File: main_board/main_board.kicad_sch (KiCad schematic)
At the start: 96 parts, among them J1 3.5mm Jack, J18 Conn_01x15_Female, J19 Conn_01x15_Female, J2 3.5mm Jack, J20 Conn_01x02_Male, J21 OLED Pins, J3 3.5mm Jack, J4 3.5mm Jack, J5 Display Header, J6 EU Power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

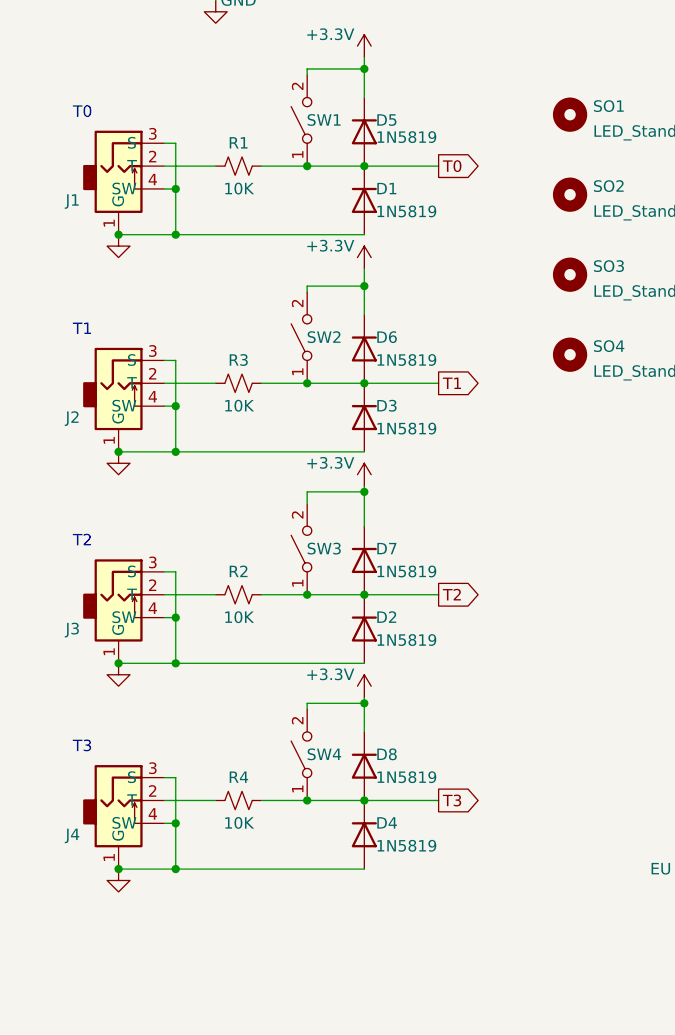
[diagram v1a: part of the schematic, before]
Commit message: Adds debounce caps to trigger inputs
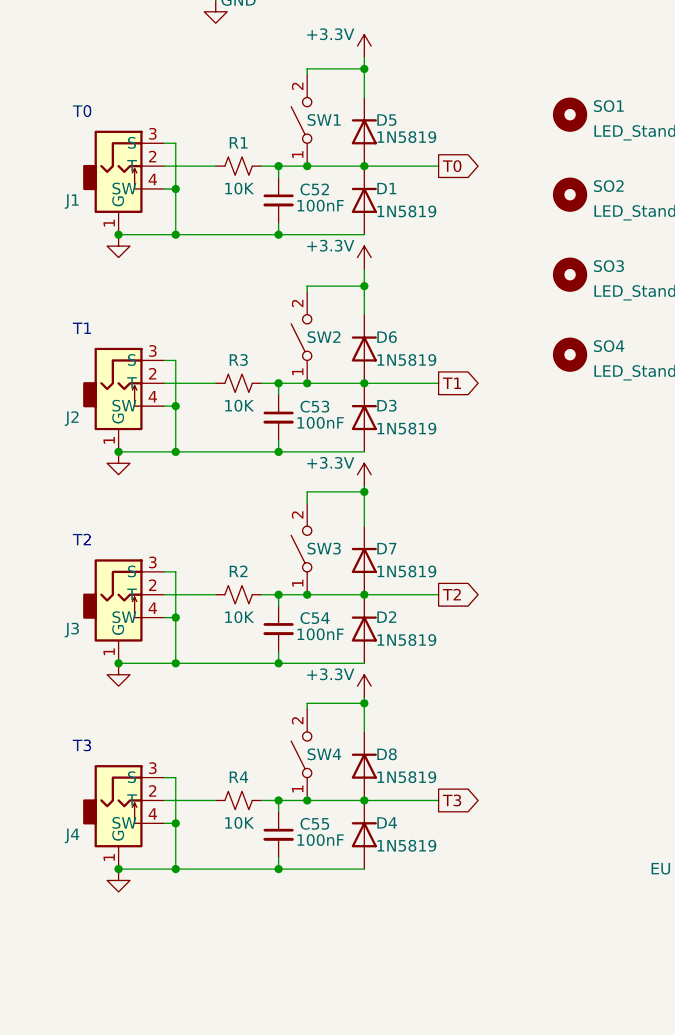
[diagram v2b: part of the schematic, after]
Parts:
- added C52, C53, C54, C55: 100nF, Capacitor_SMD:C_0805_2012Metric_Pad1.18x1.45mm_HandSolder, symbol Device:C_Small
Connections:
- net GND: now also C52.2, C53.2, C54.2, C55.2
- net T0: now also C52.1
- net T1: now also C53.1
- net T2: now also C54.1
- net T3: now also C55.1

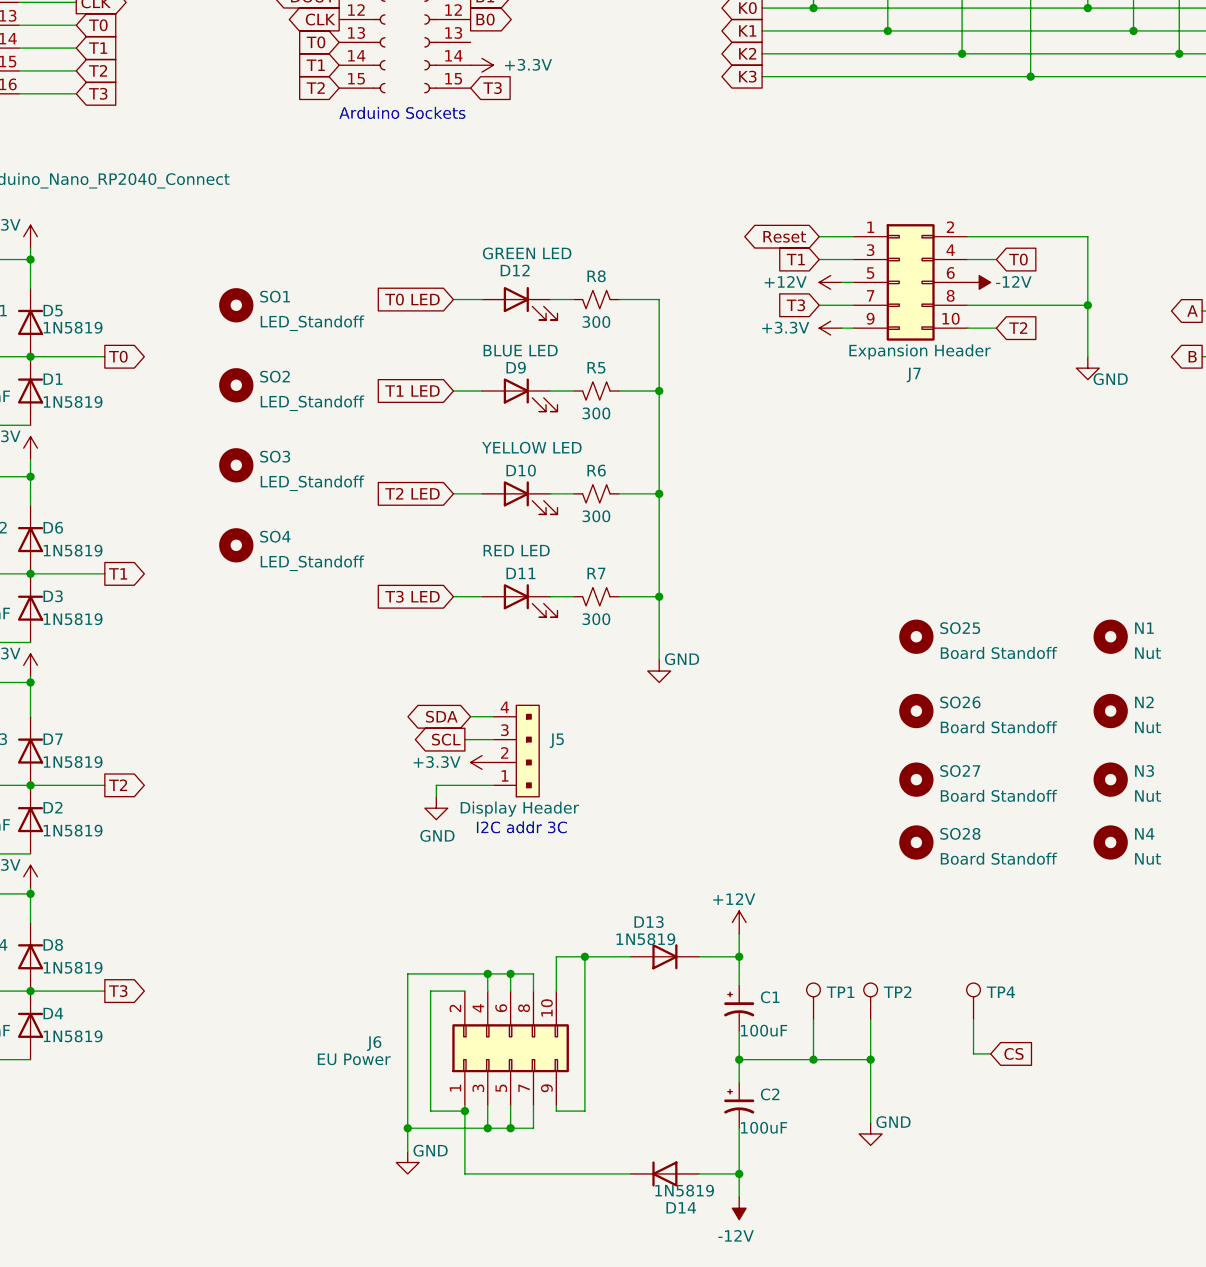
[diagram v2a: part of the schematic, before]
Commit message: Updates main_board, uses generate_boms.bat
Updates reverse protection circuitry on main board.
Updates 3.3V reference circuitry.
Uses generate_boms and retires .xlsx BOM files.
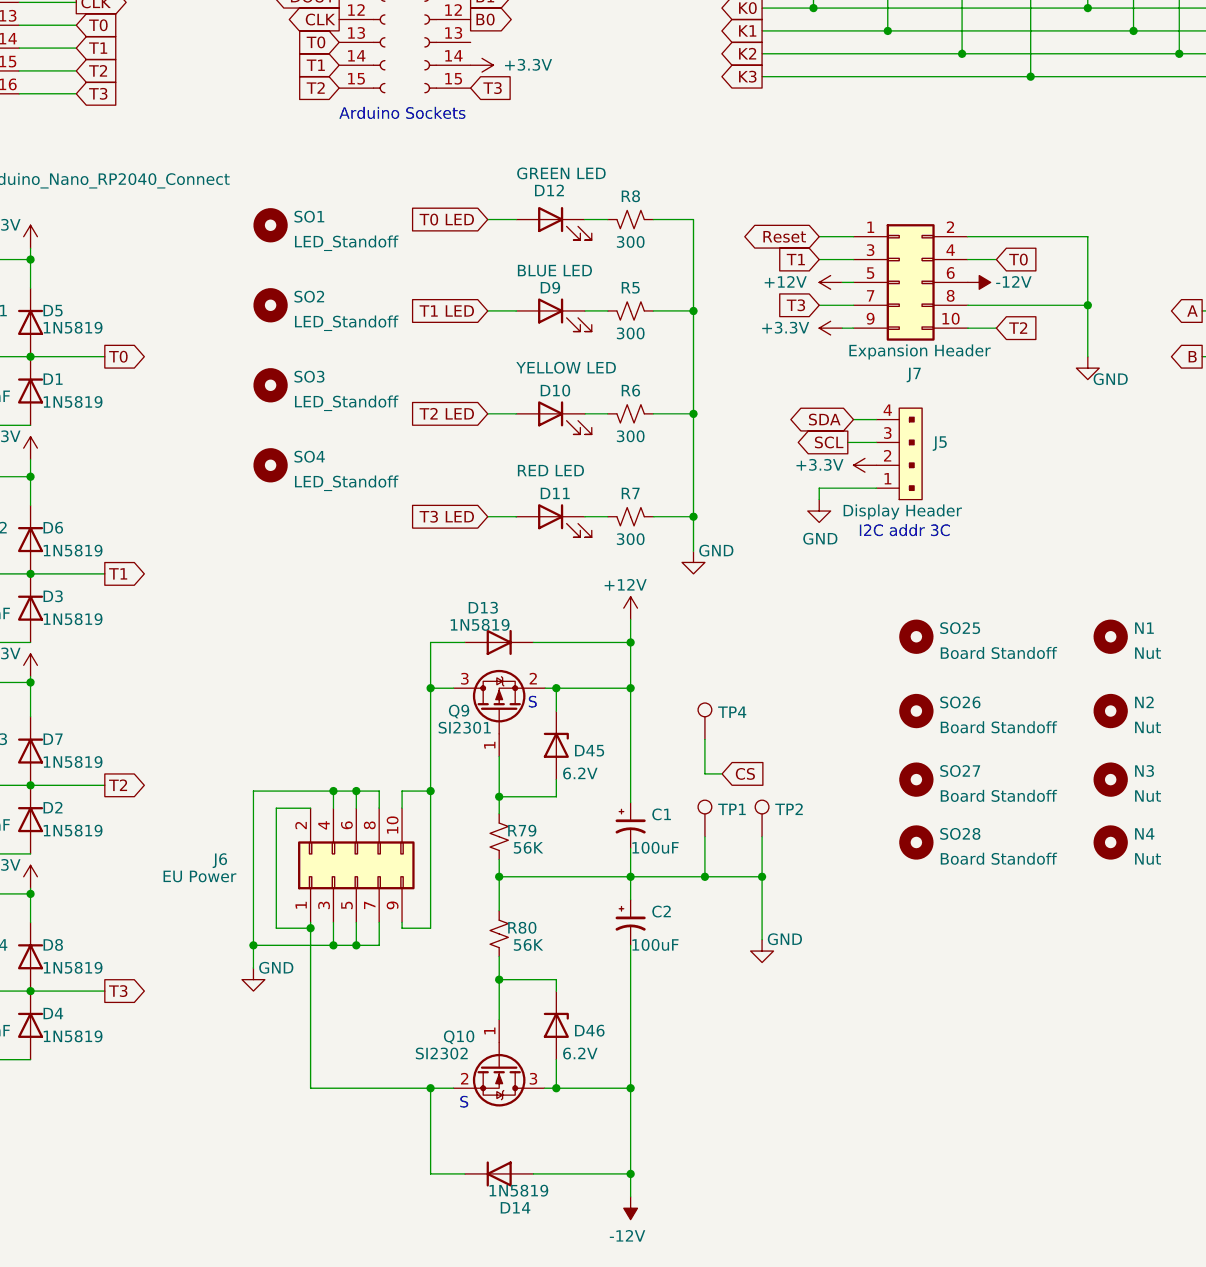
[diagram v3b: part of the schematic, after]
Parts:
- added D45, D46: 6.2V, Diode_SMD:D_SOD-323, symbol Diode:BZX384-xxx
- added Q10: SI2302, Package_TO_SOT_SMD:SOT-23, symbol Transistor_FET:2N7002
- added Q9: SI2301, Package_TO_SOT_SMD:SOT-23, symbol Transistor_FET:Si2371EDS
- added R79, R80: 56K, Resistor_SMD:R_0603_1608Metric, symbol Device:R_Small_US
- C1, C2:  LCSC Part # C2887272 -> (none); LCSC Part # (none) -> C2887272
- C11, C12:  LCSC Part # C1710 -> (none); LCSC Part # (none) -> C1710
- C30, C34, C52, C53, C54, C55:  LCSC Part # C49678 -> (none); LCSC Part # (none) -> C49678
- C7:  LCSC Part # C28323 -> (none); LCSC Part # (none) -> C28323
- D1, D13, D14, D2, D3, D4, D5, D6, D7, D8:  LCSC Part # C191023 -> (none); LCSC Part # (none) -> C191023
- J18, J19:  LCSC Part # C2932676 -> (none); LCSC Part # (none) -> C2932676
- J20:  LCSC Part # C492401 -> (none); LCSC Part # (none) -> C492401
- J6, J7:  LCSC Part # C115170 -> (none); LCSC Part # (none) -> C115170
- R1, R125, R126, R127, R128, R2, R3, R4, R66, R67, R68:  LCSC Part # C17414 -> (none); LCSC Part # (none) -> C17414
- R5, R6, R7, R8:  LCSC Part # C17617 -> (none); LCSC Part # (none) -> C17617
- TP1, TP2:  LCSC Part # C2906764 -> (none); LCSC Part # (none) -> C2906764
- TP4:  LCSC Part # C238123 -> (none); LCSC Part # (none) -> C238123
- U16:  LCSC Part # C47538 -> (none); LCSC Part # (none) -> C47538
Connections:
- net +12V: now also D45.1 (K), Q9.2 (S)
- net -12V: now also D46.2 (A), Q10.3 (D)
- net GND: now also R79.2, R80.1
- net at D13.2 (A), J6.10 (Pin_10), J6.9 (Pin_9): now also Q9.3 (D)
- net at D14.1 (K), J6.1 (Pin_1), J6.2 (Pin_2): now also Q10.2 (S)
- new net: D46.1 (K), Q10.1 (G), R80.2
- new net: D45.2 (A), Q9.1 (G), R79.1
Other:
- note added: "S"
- moved on the sheet: C1, C2, D10, D11, D12, D13, D14, D9, J5, J6, R5, R6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

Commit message: Rev 4.2 of board
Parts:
- J6, J7: LCSC Part # C115170 -> C492422
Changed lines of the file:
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@@
       (effects (font (size 1.27 1.27)) hide)
     )
-    (property "LCSC Part #" "C115170" (id 5) (at 152.4 87.63 0)
+    (property "LCSC Part #" "C492422" (id 5) (at 152.4 87.63 0)
       (effects (font (size 1.27 1.27)) hide)
     )
@@
       (effects (font (size 1.27 1.27)) hide)
     )
-    (property "LCSC Part #" "C115170" (id 5) (at 92.075 153.67 0)
+    (property "LCSC Part #" "C492422" (id 5) (at 92.075 153.67 0)
       (effects (font (size 1.27 1.27)) hide)
     )
@@
     )
     (path "/b200c1d4-b772-4a0d-a7bc-c10bcb241496/da91d24c-235c-487e-8a89-c861581e141b"
-      (reference "U13") (unit 1) (value "DG412xY") (footprint "Package_SO:SOIC-16_3.9x9.9mm_P1.27mm")
+      (reference "U13") (unit 1) (value "DG412DY-E3") (footprint "Package_SO:SOIC-16_3.9x9.9mm_P1.27mm")
     )
     (path "/b200c1d4-b772-4a0d-a7bc-c10bcb241496/4d86a335-e2f3-43e1-bfbb-9bbbf85afd83"
-      (reference "U13") (unit 2) (value "DG412xY") (footprint "Package_SO:SOIC-16_3.9x9.9mm_P1.27mm")
+      (reference "U13") (unit 2) (value "DG412DY-E3") (footprint "Package_SO:SOIC-16_3.9x9.9mm_P1.27mm")
     )
     (path "/b200c1d4-b772-4a0d-a7bc-c10bcb241496/4c813f4a-7d60-4bf9-a697-cffeff5134b5"
-      (reference "U13") (unit 3) (value "DG412xY") (footprint "Package_SO:SOIC-16_3.9x9.9mm_P1.27mm")
+      (reference "U13") (unit 3) (value "DG412DY-E3") (footprint "Package_SO:SOIC-16_3.9x9.9mm_P1.27mm")
     )
     (path "/b200c1d4-b772-4a0d-a7bc-c10bcb241496/87c697e6-3b77-4484-9517-8dc7c9b0f1d4"
-      (reference "U13") (unit 4) (value "DG412xY") (footprint "Package_SO:SOIC-16_3.9x9.9mm_P1.27mm")
+      (reference "U13") (unit 4) (value "DG412DY-E3") (footprint "Package_SO:SOIC-16_3.9x9.9mm_P1.27mm")
     )
     (path "/b200c1d4-b772-4a0d-a7bc-c10bcb241496/2c3bee7b-576b-4f00-aba9-231f47c1ce9c"
-      (reference "U13") (unit 5) (value "DG412xY") (footprint "Package_SO:SOIC-16_3.9x9.9mm_P1.27mm")
+      (reference "U13") (unit 5) (value "DG412DY-E3") (footprint "Package_SO:SOIC-16_3.9x9.9mm_P1.27mm")
     )
     (path "/eae55a42-d110-46e1-b06f-560b3d6a7f91/a5b41785-6602-47dd-88c9-fe5b8067460e"
@@
     )
     (path "/b200c1d4-b772-4a0d-a7bc-c10bcb241496/014b02a6-58b3-4f97-b161-484c3f4529db"
-      (reference "U24") (unit 1) (value "DG412xY") (footprint "Package_SO:SOIC-16_3.9x9.9mm_P1.27mm")
+      (reference "U24") (unit 1) (value "DG412DY-E3") (footprint "Package_SO:SOIC-16_3.9x9.9mm_P1.27mm")
     )
     (path "/b200c1d4-b772-4a0d-a7bc-c10bcb241496/9f9d1f6f-7507-4bd1-b7c3-1eb7cae036e5"
-      (reference "U24") (unit 2) (value "DG412xY") (footprint "Package_SO:SOIC-16_3.9x9.9mm_P1.27mm")
+      (reference "U24") (unit 2) (value "DG412DY-E3") (footprint "Package_SO:SOIC-16_3.9x9.9mm_P1.27mm")
     )
     (path "/b200c1d4-b772-4a0d-a7bc-c10bcb241496/0ef053cc-6cbc-480a-97da-ffd86eed29bd"
-      (reference "U24") (unit 3) (value "DG412xY") (footprint "Package_SO:SOIC-16_3.9x9.9mm_P1.27mm")
+      (reference "U24") (unit 3) (value "DG412DY-E3") (footprint "Package_SO:SOIC-16_3.9x9.9mm_P1.27mm")
     )
     (path "/b200c1d4-b772-4a0d-a7bc-c10bcb241496/f9466c72-e334-45f8-ab36-33d7247619a7"
-      (reference "U24") (unit 4) (value "DG412xY") (footprint "Package_SO:SOIC-16_3.9x9.9mm_P1.27mm")
+      (reference "U24") (unit 4) (value "DG412DY-E3") (footprint "Package_SO:SOIC-16_3.9x9.9mm_P1.27mm")
     )
     (path "/b200c1d4-b772-4a0d-a7bc-c10bcb241496/56818c14-9875-4852-83e7-b24bf77170c1"
-      (reference "U24") (unit 5) (value "DG412xY") (footprint "Package_SO:SOIC-16_3.9x9.9mm_P1.27mm")
-    )
-  )
+      (reference "U24") (unit 5) (value "DG412DY-E3") (footprint "Package_SO:SOIC-16_3.9x9.9mm_P1.27mm")
+    )
+  )

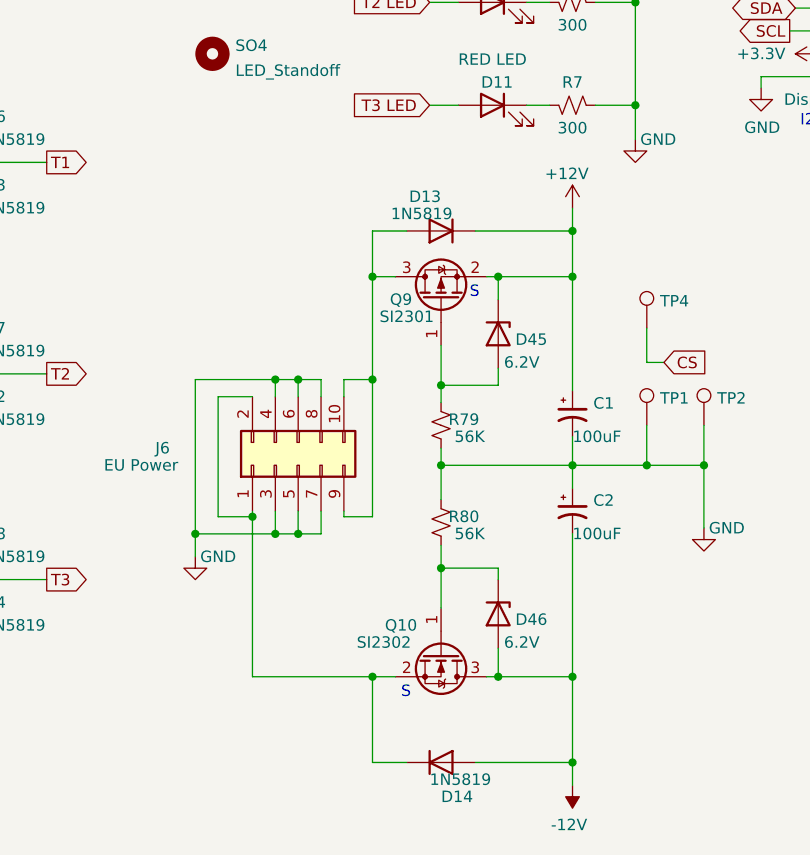
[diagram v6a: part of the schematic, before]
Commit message: Goes to diodes for reverse power protection
Re-layout for better noise performance.
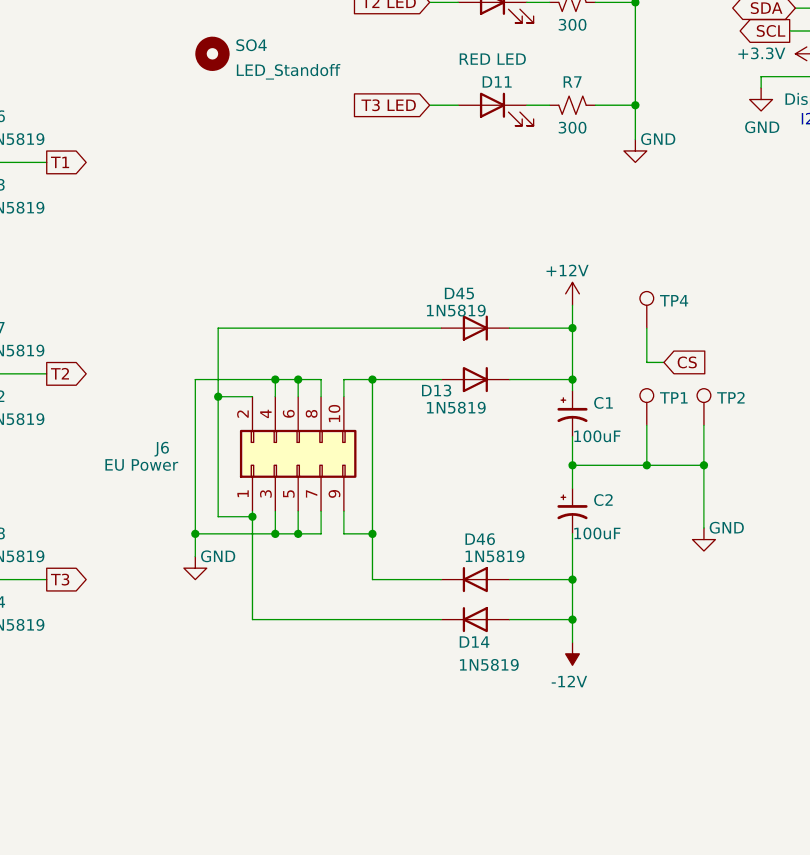
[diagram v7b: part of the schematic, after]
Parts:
- removed D45, D46: 6.2V, Diode_SMD:D_SOD-323, symbol Diode:BZX384-xxx
- removed Q10: SI2302, Package_TO_SOT_SMD:SOT-23, symbol Transistor_FET:2N7002
- removed Q9: SI2301, Package_TO_SOT_SMD:SOT-23, symbol Transistor_FET:Si2371EDS
- removed R79, R80: 56K, Resistor_SMD:R_0603_1608Metric, symbol Device:R_Small_US
- added D45, D46: 1N5819, Diode_SMD:D_0805_2012Metric_Pad1.15x1.40mm_HandSolder, symbol Diode:1N4148
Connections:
- net +12V: now also D45.1 (K)
- net -12V: now also D46.2 (A)
- net at D13.2 (A), J6.10 (Pin_10), J6.9 (Pin_9): now also D46.1 (K)
- net at D14.1 (K), J6.1 (Pin_1), J6.2 (Pin_2): now also D45.2 (A)
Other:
- note removed: "S"
- moved on the sheet: D13, D14
